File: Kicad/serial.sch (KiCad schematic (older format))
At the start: 9 parts, among them J801 Conn_02x05, J802 DB9_Male_MountingHoles, U801 ST3232CDR

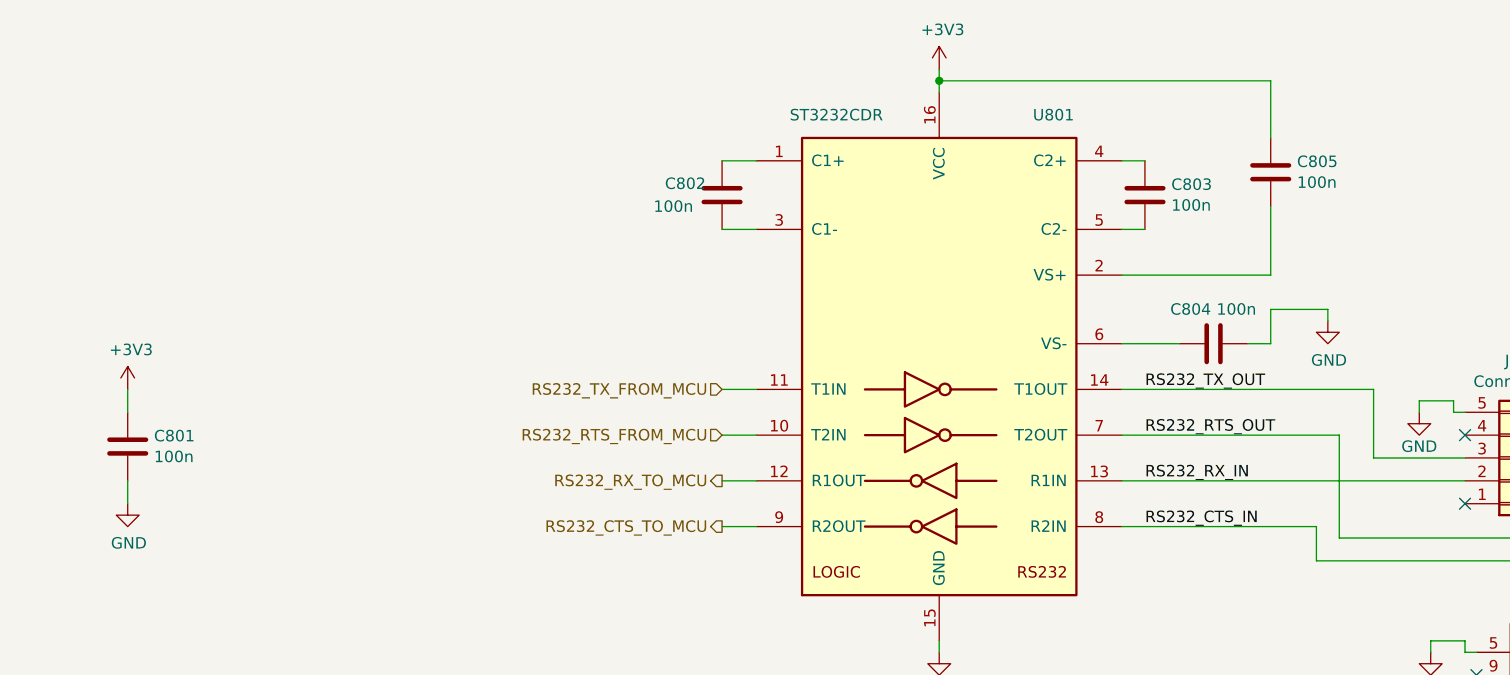
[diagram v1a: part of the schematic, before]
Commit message: Fix V+ capacitor - must go to ground, not Vcc.
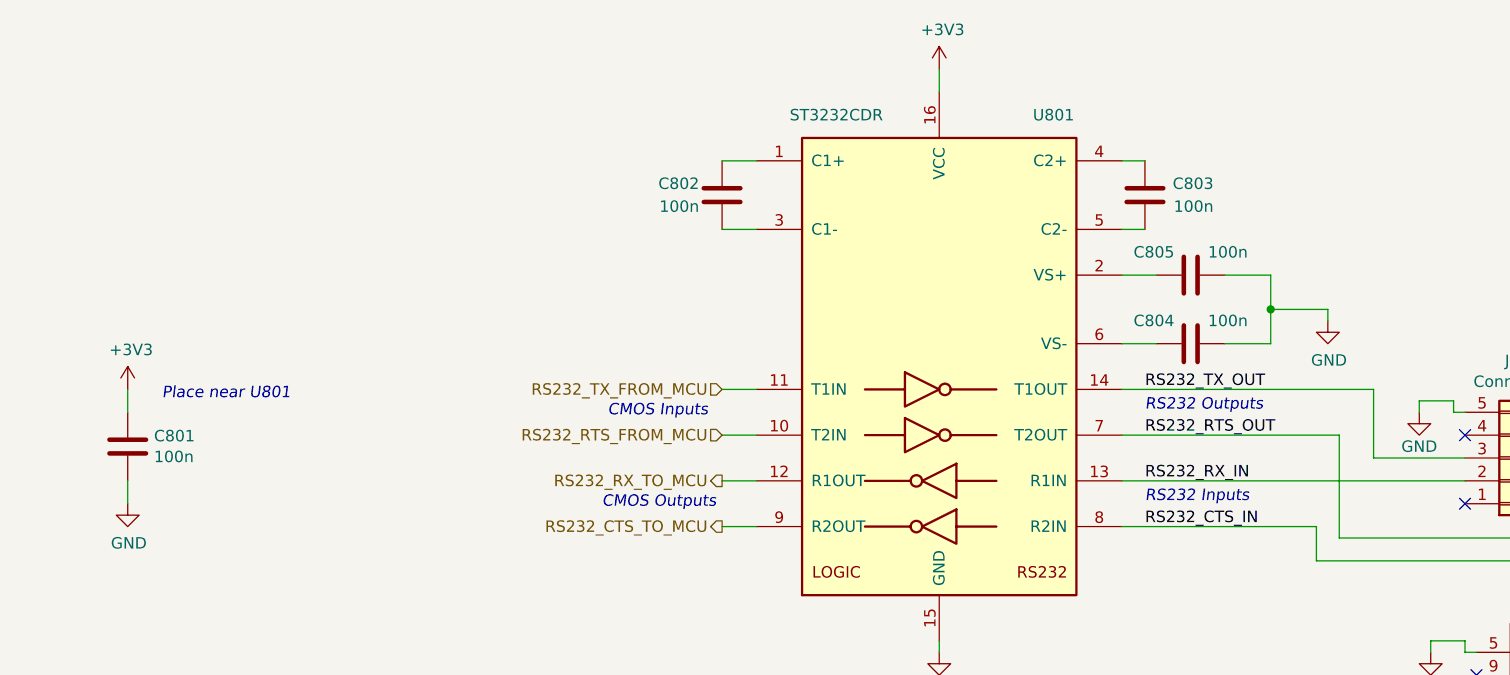
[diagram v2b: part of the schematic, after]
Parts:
- U801: footprint Package_SO:SOP-16_4.4x10.4mm_P1.27mm -> Package_SO:SO-16_5.3x10.2mm_P1.27mm
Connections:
- wire segments 50 -> 48
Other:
- note added: "CMOS Inputs"
- note added: "CMOS Outputs"
- note added: "Place near U801"
- note added: "RS232 Inputs"
- note added: "RS232 Outputs"
- moved on the sheet: C804, C805
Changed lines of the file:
@@
 F 0 "U801" H 5950 4150 50  0000 C CNN
 F 1 "ST3232CDR" H 5000 4150 50  0000 C CNN
-F 2 "Package_SO:SOP-16_4.4x10.4mm_P1.27mm" H 5500 2000 50  0001 L CNN
+F 2 "Package_SO:SO-16_5.3x10.2mm_P1.27mm" H 5500 2000 50  0001 L CNN
 F 3 "https://www.st.com/content/ccc/resource/technical/document/datasheet/group1/40/2c/7f/62/3a/3f/47/3c/CD00002253/files/CD00002253.pdf/jcr:content/translations/en.CD00002253.pdf" H 5450 3150 50  0001 C CNN
 F 4 "ST" H 5450 3050 50  0001 C CNN "Manufacturer"
@@
 U 1 1 5E181E57
 P 6350 2300
-F 0 "C803" H 6465 2346 50  0000 L CNN
-F 1 "100n" H 6465 2255 50  0000 L CNN
+F 0 "C803" H 6650 2350 50  0000 R CNN
+F 1 "100n" H 6650 2250 50  0000 R CNN
 F 2 "Capacitor_SMD:C_0805_2012Metric_Pad1.15x1.40mm_HandSolder" H 6388 2150 50  0001 C CNN
 F 3 "~" H 6350 2300 50  0001 C CNN
@@
 L Device:C C804
 U 1 1 5E182C3F
-P 6650 2950
-F 0 "C804" V 6500 2850 50  0000 C CNN
-F 1 "100n" V 6500 3050 50  0000 C CNN
-F 2 "Capacitor_SMD:C_0805_2012Metric_Pad1.15x1.40mm_HandSolder" H 6688 2800 50  0001 C CNN
-F 3 "~" H 6650 2950 50  0001 C CNN
-F 4 "Vishay" H -150 -600 50  0001 C CNN "Manufacturer"
-F 5 "K104K15X7RF5TL2" H -150 -600 50  0001 C CNN "mpn"
-F 6 "0" H 6650 2950 50  0001 C CNN "DNP"
-F 7 " BC1150CT-ND" H 6650 2950 50  0001 C CNN "Digikey"
-	1    6650 2950
+P 6550 2950
+F 0 "C804" V 6450 2700 50  0000 L CNN
+F 1 "100n" V 6450 3200 50  0000 R CNN
+F 2 "Capacitor_SMD:C_0805_2012Metric_Pad1.15x1.40mm_HandSolder" H 6588 2800 50  0001 C CNN
+F 3 "~" H 6550 2950 50  0001 C CNN
+F 4 "Vishay" H -250 -600 50  0001 C CNN "Manufacturer"
+F 5 "K104K15X7RF5TL2" H -250 -600 50  0001 C CNN "mpn"
+F 6 "0" H 6550 2950 50  0001 C CNN "DNP"
+F 7 " BC1150CT-ND" H 6550 2950 50  0001 C CNN "Digikey"
+	1    6550 2950
 	0    1    1    0
-$EndComp
-$Comp
-L Device:C C802
-U 1 1 5E182DBA
-P 4500 2300
-F 0 "C802" H 4750 2250 50  0000 R CNN
-F 1 "100n" H 4800 2350 50  0000 R CNN
-F 2 "Capacitor_SMD:C_0805_2012Metric_Pad1.15x1.40mm_HandSolder" H 4538 2150 50  0001 C CNN
-F 3 "~" H 4500 2300 50  0001 C CNN
-F 4 "Vishay" H -150 -600 50  0001 C CNN "Manufacturer"
-F 5 "K104K15X7RF5TL2" H -150 -600 50  0001 C CNN "mpn"
-F 6 "0" H 4500 2300 50  0001 C CNN "DNP"
-F 7 " BC1150CT-ND" H 4500 2300 50  0001 C CNN "Digikey"
-	1    4500 2300
-	-1   0    0    1
 $EndComp
 $Comp
@@
 	1    0    0    -1
 $EndComp
-Wire Wire Line
-	5450 1750 5450 1800
 $Comp
 L power:+3V3 #PWR0801
@@
 $EndComp
 Wire Wire Line
-	6250 2950 6500 2950
-Wire Wire Line
-	6800 2950 6900 2950
+	6250 2950 6400 2950
+Wire Wire Line
+	6700 2950 6900 2950
 Wire Wire Line
 	6900 2950 6900 2800
@@
 	6900 2800 7150 2800
 Wire Wire Line
-	5450 1800 6900 1800
-Connection ~ 5450 1800
-Wire Wire Line
-	5450 1800 5450 1850
-Wire Wire Line
 	6250 2150 6350 2150
 Wire Wire Line
@@
 Wire Wire Line
 	4500 2450 4650 2450
-$Comp
-L Device:C C805
-U 1 1 5E188858
-P 6900 2200
-F 0 "C805" H 7015 2246 50  0000 L CNN
-F 1 "100n" H 7015 2155 50  0000 L CNN
-F 2 "Capacitor_SMD:C_0805_2012Metric_Pad1.15x1.40mm_HandSolder" H 6938 2050 50  0001 C CNN
-F 3 "~" H 6900 2200 50  0001 C CNN
-F 4 "Vishay" H -150 -600 50  0001 C CNN "Manufacturer"
-F 5 "K104K15X7RF5TL2" H -150 -600 50  0001 C CNN "mpn"
-F 6 "0" H 6900 2200 50  0001 C CNN "DNP"
-F 7 " BC1150CT-ND" H 6900 2200 50  0001 C CNN "Digikey"
-	1    6900 2200
-	1    0    0    -1
-$EndComp
-Wire Wire Line
-	6900 1800 6900 2050
-Wire Wire Line
-	6900 2350 6900 2650
-Wire Wire Line
-	6250 2650 6900 2650
 $Comp
 L power:GND #PWR0804
@@
 	7800 4900 7250 4900
 Wire Wire Line
-	7800 4800 7250 4800
-Wire Wire Line
 	7800 4700 7250 4700
-Wire Wire Line
-	7800 4600 7250 4600
 $Comp
 L power:GND #PWR0807
@@
 Wire Wire Line
 	8100 5350 8100 5300
+Wire Wire Line
+	5450 1750 5450 1850
+Wire Wire Line
+	6700 2650 6900 2650
+Wire Wire Line
+	6900 2650 6900 2800
+Connection ~ 6900 2800
+Wire Wire Line
+	6250 2650 6400 2650
+$Comp
+L Device:C C805
+U 1 1 5E188858
+P 6550 2650
+F 0 "C805" V 6450 2400 50  0000 L CNN
+F 1 "100n" V 6450 2900 50  0000 R CNN
+F 2 "Capacitor_SMD:C_0805_2012Metric_Pad1.15x1.40mm_HandSolder" H 6588 2500 50  0001 C CNN
+F 3 "~" H 6550 2650 50  0001 C CNN
+F 4 "Vishay" H -500 -150 50  0001 C CNN "Manufacturer"
+F 5 "K104K15X7RF5TL2" H -500 -150 50  0001 C CNN "mpn"
+F 6 "0" H 6550 2650 50  0001 C CNN "DNP"
+F 7 " BC1150CT-ND" H 6550 2650 50  0001 C CNN "Digikey"
+	1    6550 2650
+	0    1    1    0
+$EndComp
+$Comp
+L Device:C C802
+U 1 1 5E182DBA
+P 4500 2300
+F 0 "C802" H 4600 2250 50  0000 L CNN
+F 1 "100n" H 4600 2350 50  0000 L CNN
+F 2 "Capacitor_SMD:C_0805_2012Metric_Pad1.15x1.40mm_HandSolder" H 4538 2150 50  0001 C CNN
+F 3 "~" H 4500 2300 50  0001 C CNN
+F 4 "Vishay" H -150 -600 50  0001 C CNN "Manufacturer"
+F 5 "K104K15X7RF5TL2" H -150 -600 50  0001 C CNN "mpn"
+F 6 "0" H 4500 2300 50  0001 C CNN "DNP"
+F 7 " BC1150CT-ND" H 4500 2300 50  0001 C CNN "Digikey"
+	1    4500 2300
+	-1   0    0    1
+$EndComp
+Text Notes 2050 3200 0    50   Italic 0
+Place near U801
+Text Notes 4000 3275 0    50   Italic 0
+CMOS Inputs
+Text Notes 3975 3675 0    50   Italic 0
+CMOS Outputs
+Text Notes 6350 3250 0    50   Italic 0
+RS232 Outputs
+Text Notes 6350 3650 0    50   Italic 0
+RS232 Inputs
+Wire Wire Line
+	7800 4800 7250 4800
+Wire Wire Line
+	7800 4600 7250 4600
 $EndSCHEMATC

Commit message: Replaced NUC029 (TSSOP) with KE04 (SOIC).
Also updated the BOM with some part nos.
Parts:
- C801, C802, C803, C804, C805: Digikey BC1150CT-ND -> BC1150CT-ND; MPN (none) -> K104K15X7RF5TL2; mpn K104K15X7RF5TL2 -> (none)
- J801: Digikey (none) -> ED1543-ND; MPN (none) -> 302-S101; mpn 302-S101 -> (none)
- U801: Digikey (none) -> 497-3731-1-ND; MPN (none) -> ST3232CDR; mpn ST3232CDR -> (none)
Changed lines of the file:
@@
 F 3 "https://www.st.com/content/ccc/resource/technical/document/datasheet/group1/40/2c/7f/62/3a/3f/47/3c/CD00002253/files/CD00002253.pdf/jcr:content/translations/en.CD00002253.pdf" H 5450 3150 50  0001 C CNN
 F 4 "ST" H 5450 3050 50  0001 C CNN "Manufacturer"
-F 5 "ST3232CDR" H 5450 3050 50  0001 C CNN "mpn"
+F 5 "" H 5450 3050 50  0001 C CNN "mpn"
 F 6 "0" H 5450 3050 50  0001 C CNN "DNP"
+F 7 "497-3731-1-ND" H 5450 3050 50  0001 C CNN "Digikey"
+F 8 "ST3232CDR" H 5450 3050 50  0001 C CNN "MPN"
 	1    5450 3050
 	1    0    0    -1
@@
 F 3 "~" H 6350 2300 50  0001 C CNN
 F 4 "Vishay" H -150 -600 50  0001 C CNN "Manufacturer"
-F 5 "K104K15X7RF5TL2" H -150 -600 50  0001 C CNN "mpn"
+F 5 "" H -150 -600 50  0001 C CNN "mpn"
 F 6 "0" H 6350 2300 50  0001 C CNN "DNP"
-F 7 " BC1150CT-ND" H 6350 2300 50  0001 C CNN "Digikey"
+F 7 "BC1150CT-ND" H 6350 2300 50  0001 C CNN "Digikey"
+F 8 "K104K15X7RF5TL2" H 6350 2300 50  0001 C CNN "MPN"
 	1    6350 2300
 	1    0    0    -1
@@
 F 3 "~" H 6550 2950 50  0001 C CNN
 F 4 "Vishay" H -250 -600 50  0001 C CNN "Manufacturer"
-F 5 "K104K15X7RF5TL2" H -250 -600 50  0001 C CNN "mpn"
+F 5 "" H -250 -600 50  0001 C CNN "mpn"
 F 6 "0" H 6550 2950 50  0001 C CNN "DNP"
-F 7 " BC1150CT-ND" H 6550 2950 50  0001 C CNN "Digikey"
+F 7 "BC1150CT-ND" H 6550 2950 50  0001 C CNN "Digikey"
+F 8 "K104K15X7RF5TL2" H 6550 2950 50  0001 C CNN "MPN"
 	1    6550 2950
 	0    1    1    0
@@
 F 3 "~" H 1900 3400 50  0001 C CNN
 F 4 "Vishay" H -1450 300 50  0001 C CNN "Manufacturer"
-F 5 "K104K15X7RF5TL2" H -1450 300 50  0001 C CNN "mpn"
+F 5 "" H -1450 300 50  0001 C CNN "mpn"
 F 6 "0" H 1900 3400 50  0001 C CNN "DNP"
-F 7 " BC1150CT-ND" H 1900 3400 50  0001 C CNN "Digikey"
+F 7 "BC1150CT-ND" H 1900 3400 50  0001 C CNN "Digikey"
+F 8 "K104K15X7RF5TL2" H 1900 3400 50  0001 C CNN "MPN"
 	1    1900 3400
 	-1   0    0    1
@@
 F 3 "~" H 7950 3450 50  0001 C CNN
 F 4 "On Shore Technology" H 7950 3450 50  0001 C CNN "Manufacturer"
-F 5 "302-S101" H 7950 3450 50  0001 C CNN "mpn"
+F 5 "" H 7950 3450 50  0001 C CNN "mpn"
 F 6 "0" H 7950 3450 50  0001 C CNN "DNP"
+F 7 "ED1543-ND" H 7950 3450 50  0001 C CNN "Digikey"
+F 8 "302-S101" H 7950 3450 50  0001 C CNN "MPN"
 	1    7950 3450
 	1    0    0    1
@@
 F 3 "~" H 6550 2650 50  0001 C CNN
 F 4 "Vishay" H -500 -150 50  0001 C CNN "Manufacturer"
-F 5 "K104K15X7RF5TL2" H -500 -150 50  0001 C CNN "mpn"
+F 5 "" H -500 -150 50  0001 C CNN "mpn"
 F 6 "0" H 6550 2650 50  0001 C CNN "DNP"
-F 7 " BC1150CT-ND" H 6550 2650 50  0001 C CNN "Digikey"
+F 7 "BC1150CT-ND" H 6550 2650 50  0001 C CNN "Digikey"
+F 8 "K104K15X7RF5TL2" H 6550 2650 50  0001 C CNN "MPN"
 	1    6550 2650
 	0    1    1    0
@@
 F 3 "~" H 4500 2300 50  0001 C CNN
 F 4 "Vishay" H -150 -600 50  0001 C CNN "Manufacturer"
-F 5 "K104K15X7RF5TL2" H -150 -600 50  0001 C CNN "mpn"
+F 5 "" H -150 -600 50  0001 C CNN "mpn"
 F 6 "0" H 4500 2300 50  0001 C CNN "DNP"
-F 7 " BC1150CT-ND" H 4500 2300 50  0001 C CNN "Digikey"
+F 7 "BC1150CT-ND" H 4500 2300 50  0001 C CNN "Digikey"
+F 8 "K104K15X7RF5TL2" H 4500 2300 50  0001 C CNN "MPN"
 	1    4500 2300
 	-1   0    0    1

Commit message: Bring in R2R DAC from Neotron-9X schematic.
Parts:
- renumbered C802 to C801, C803 to C802, C805 to C803, C801 to C805
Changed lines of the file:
@@
 $Descr A4 11693 8268
 encoding utf-8
-Sheet 7 9
+Sheet 7 12
 Title "Neotron Common Hardware - Serial Port"
 Date "2021-01-01"
@@
 RS232_RTS_OUT
 $Comp
-L power:GND #PWR0805
+L power:GND #PWR0802
 U 1 1 5E180507
 P 7150 2850
-F 0 "#PWR0805" H 7150 2600 50  0001 C CNN
+F 0 "#PWR0802" H 7150 2600 50  0001 C CNN
 F 1 "GND" H 7155 2677 50  0000 C CNN
 F 2 "" H 7150 2850 50  0001 C CNN
@@
 	7150 2850 7150 2800
 $Comp
-L Device:C C803
+L Device:C C802
 U 1 1 5E181E57
 P 6350 2300
-F 0 "C803" H 6650 2350 50  0000 R CNN
+F 0 "C802" H 6650 2350 50  0000 R CNN
 F 1 "100n" H 6650 2250 50  0000 R CNN
 F 2 "Capacitor_SMD:C_0805_2012Metric_Pad1.15x1.40mm_HandSolder" H 6388 2150 50  0001 C CNN
@@
 $EndComp
 $Comp
-L Device:C C801
+L Device:C C805
 U 1 1 5E183108
 P 1900 3400
-F 0 "C801" H 1785 3354 50  0000 R CNN
+F 0 "C805" H 1785 3354 50  0000 R CNN
 F 1 "100n" H 1785 3445 50  0000 R CNN
 F 2 "Capacitor_SMD:C_0805_2012Metric_Pad1.15x1.40mm_HandSolder" H 1938 3250 50  0001 C CNN
@@
 $EndComp
 $Comp
-L power:+3V3 #PWR0803
+L power:+3V3 #PWR0801
 U 1 1 5E183A22
 P 5450 1750
-F 0 "#PWR0803" H 5450 1600 50  0001 C CNN
+F 0 "#PWR0801" H 5450 1600 50  0001 C CNN
 F 1 "+3V3" H 5465 1923 50  0000 C CNN
 F 2 "" H 5450 1750 50  0001 C CNN
@@
 $EndComp
 $Comp
-L power:+3V3 #PWR0801
+L power:+3V3 #PWR0803
 U 1 1 5E18439B
 P 1900 3150
-F 0 "#PWR0801" H 1900 3000 50  0001 C CNN
+F 0 "#PWR0803" H 1900 3000 50  0001 C CNN
 F 1 "+3V3" H 1915 3323 50  0000 C CNN
 F 2 "" H 1900 3150 50  0001 C CNN
@@
 $EndComp
 $Comp
-L power:GND #PWR0802
+L power:GND #PWR0805
 U 1 1 5E1846FE
 P 1900 3650
-F 0 "#PWR0802" H 1900 3400 50  0001 C CNN
+F 0 "#PWR0805" H 1900 3400 50  0001 C CNN
 F 1 "GND" H 1905 3477 50  0000 C CNN
 F 2 "" H 1900 3650 50  0001 C CNN
@@
 	4500 2450 4650 2450
 $Comp
-L power:GND #PWR0804
+L power:GND #PWR0806
 U 1 1 5E18A6A9
 P 5450 4300
-F 0 "#PWR0804" H 5450 4050 50  0001 C CNN
+F 0 "#PWR0806" H 5450 4050 50  0001 C CNN
 F 1 "GND" H 5455 4127 50  0000 C CNN
 F 2 "" H 5450 4300 50  0001 C CNN
@@
 $EndComp
 $Comp
-L power:GND #PWR0806
+L power:GND #PWR0804
 U 1 1 5E03D39E
 P 7550 3250
-F 0 "#PWR0806" H 7550 3000 50  0001 C CNN
+F 0 "#PWR0804" H 7550 3000 50  0001 C CNN
 F 1 "GND" H 7550 3100 50  0000 C CNN
 F 2 "" H 7550 3250 50  0001 C CNN
@@
 	6250 2650 6400 2650
 $Comp
-L Device:C C805
+L Device:C C803
 U 1 1 5E188858
 P 6550 2650
-F 0 "C805" V 6450 2400 50  0000 L CNN
+F 0 "C803" V 6450 2400 50  0000 L CNN
 F 1 "100n" V 6450 2900 50  0000 R CNN
 F 2 "Capacitor_SMD:C_0805_2012Metric_Pad1.15x1.40mm_HandSolder" H 6588 2500 50  0001 C CNN
@@
 $EndComp
 $Comp
-L Device:C C802
+L Device:C C801
 U 1 1 5E182DBA
 P 4500 2300
-F 0 "C802" H 4600 2250 50  0000 L CNN
+F 0 "C801" H 4600 2250 50  0000 L CNN
 F 1 "100n" H 4600 2350 50  0000 L CNN
 F 2 "Capacitor_SMD:C_0805_2012Metric_Pad1.15x1.40mm_HandSolder" H 4538 2150 50  0001 C CNN
